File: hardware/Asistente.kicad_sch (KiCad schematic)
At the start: 11 parts, among them U2 pam8403

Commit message: hw: update PCB layout, add Gerber files and INMP441 footprint
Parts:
- C1: footprint (none) -> Capacitor_THT:CP_Radial_D10.0mm_P5.00mm
- C2, C3: footprint (none) -> Capacitor_SMD:C_0805_2012Metric
- INMP441: renamed from M1; footprint (none) -> INMP441:INMP441
- R3, R4: footprint (none) -> Resistor_SMD:R_0603_1608Metric
- U1: footprint ESP32_30pin -> ESP32_Footprints:ESP32_30pin
- U2: footprint (none) -> pam8403:pam8403
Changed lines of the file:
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@@
-		(color 0 0 0 0)
-	)
-	(junction
-		(at 85.09 106.68)
-		(diameter 0)
 		(color 0 0 0 0)
 	)
@@
 	(wire
 		(pts
-			(xy 83.82 106.68) (xy 85.09 106.68)
-		)
-		(stroke
-			(width 0)
-			(type default)
-		)
-	)
-	(wire
-		(pts
 			(xy 101.6 88.9) (xy 101.6 86.36)
 		)
@@
 	(wire
 		(pts
-			(xy 85.09 106.68) (xy 100.33 106.68)
-		)
-		(stroke
-			(width 0)
-			(type default)
-		)
-	)
-	(wire
-		(pts
 			(xy 140.97 44.45) (xy 140.97 33.02)
 		)
@@
 	(wire
 		(pts
+			(xy 83.82 106.68) (xy 100.33 106.68)
+		)
+		(stroke
+			(width 0)
+			(type default)
+		)
+	)
+	(wire
+		(pts
 			(xy 138.43 73.66) (xy 143.51 73.66)
 		)
@@
 		(pts
 			(xy 110.49 86.36) (xy 106.68 86.36)
-		)
-		(stroke
-			(width 0)
-			(type default)
-		)
-	)
-	(wire
-		(pts
-			(xy 85.09 105.41) (xy 85.09 106.68)
 		)
 		(stroke
@@
 			)
 		)
-		(property "Footprint" ""
+		(property "Footprint" "Resistor_SMD:R_0603_1608Metric"
 			(at 103.378 82.55 90)
 			(effects
@@
 			)
 		)
-		(property "Footprint" ""
+		(property "Footprint" "Capacitor_SMD:C_0805_2012Metric"
 			(at 96.52 72.39 0)
 			(effects
@@
 			)
 		)
-		(property "Footprint" ""
+		(property "Footprint" "Resistor_SMD:R_0603_1608Metric"
 			(at 98.298 82.55 90)
 			(effects
@@
 			)
 		)
-		(property "Footprint" ""
+		(property "Footprint" "Capacitor_THT:CP_Radial_D10.0mm_P5.00mm"
 			(at 101.2952 114.3 0)
 			(effects
@@
 			)
 		)
-		(property "Footprint" ""
+		(property "Footprint" "pam8403:pam8403"
 			(at 123.825 50.165 0)
 			(effects
@@
 			)
 		)
-		(property "Footprint" ""
+		(property "Footprint" "Capacitor_SMD:C_0805_2012Metric"
 			(at 101.6 72.39 0)
 			(effects
@@
 			)
 		)
-		(property "Footprint" "ESP32_30pin"
+		(property "Footprint" "ESP32_Footprints:ESP32_30pin"
 			(at 110.998 116.586 90)
 			(effects
@@
 				(path "/97dc264d-c8ec-4099-a14f-39f91d52d718"
 					(reference "U1")
-					(unit 1)
-				)
-			)
-		)
-	)
-	(symbol
-		(lib_id "power:PWR_FLAG")
-		(at 85.09 105.41 0)
-		(unit 1)
-		(exclude_from_sim no)
-		(in_bom yes)
-		(on_board yes)
-		(dnp no)
-		(fields_autoplaced yes)
-		(property "Reference" "#FLG01"
-			(at 85.09 103.505 0)
-			(effects
-				(font
-					(size 1.27 1.27)
-				)
-				(hide yes)
-			)
-		)
-		(property "Value" "PWR_FLAG"
-			(at 85.09 100.33 0)
-			(effects
-				(font
-					(size 1.27 1.27)
-				)
-			)
-		)
-		(property "Footprint" ""
-			(at 85.09 105.41 0)
-			(effects
-				(font
-					(size 1.27 1.27)
-				)
-				(hide yes)
-			)
-		)
-		(property "Datasheet" "~"
-			(at 85.09 105.41 0)
-			(effects
-				(font
-					(size 1.27 1.27)
-				)
-				(hide yes)
-			)
-		)
-		(property "Description" "Special symbol for telling ERC where power comes from"
-			(at 85.09 105.41 0)
-			(effects
-				(font
-					(size 1.27 1.27)
-				)
-				(hide yes)
-			)
-		)
-		(pin "1"
-		)
-		(instances
-			(project ""
-				(path "/97dc264d-c8ec-4099-a14f-39f91d52d718"
-					(reference "#FLG01")
 					(unit 1)
 				)
@@
 		(dnp no)
 		(fields_autoplaced yes)
-		(property "Reference" "M1"
+		(property "Reference" "INMP441"
 			(at 132.08 132.0799 0)
 			(effects
@@
 			)
 		)
-		(property "Footprint" ""
+		(property "Footprint" "INMP441:INMP441"
 			(at 124.46 133.35 0)
 			(effects
@@
 					(size 1.27 1.27)
 				)
-				(hide yes)
 			)
 		)
@@
 			(project ""
 				(path "/97dc264d-c8ec-4099-a14f-39f91d52d718"
-					(reference "M1")
+					(reference "INMP441")
 					(unit 1)
 				)

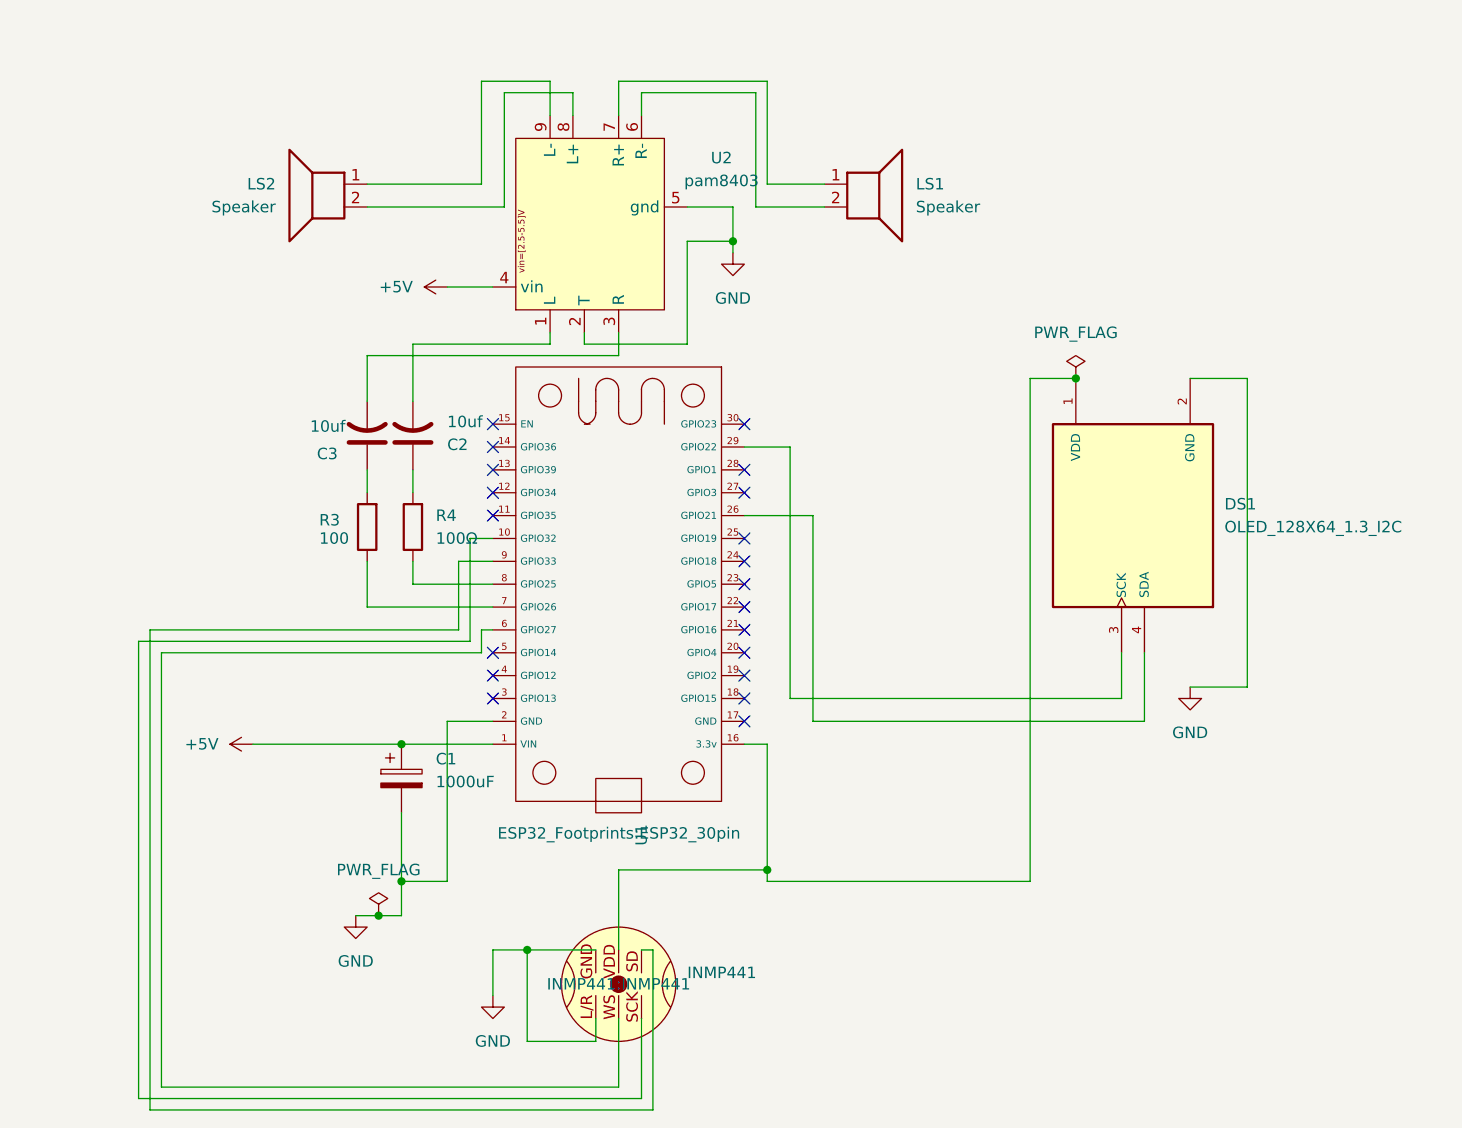
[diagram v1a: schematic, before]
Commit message: feat: add external connectors for OLED, mic and speakers, update gerber files
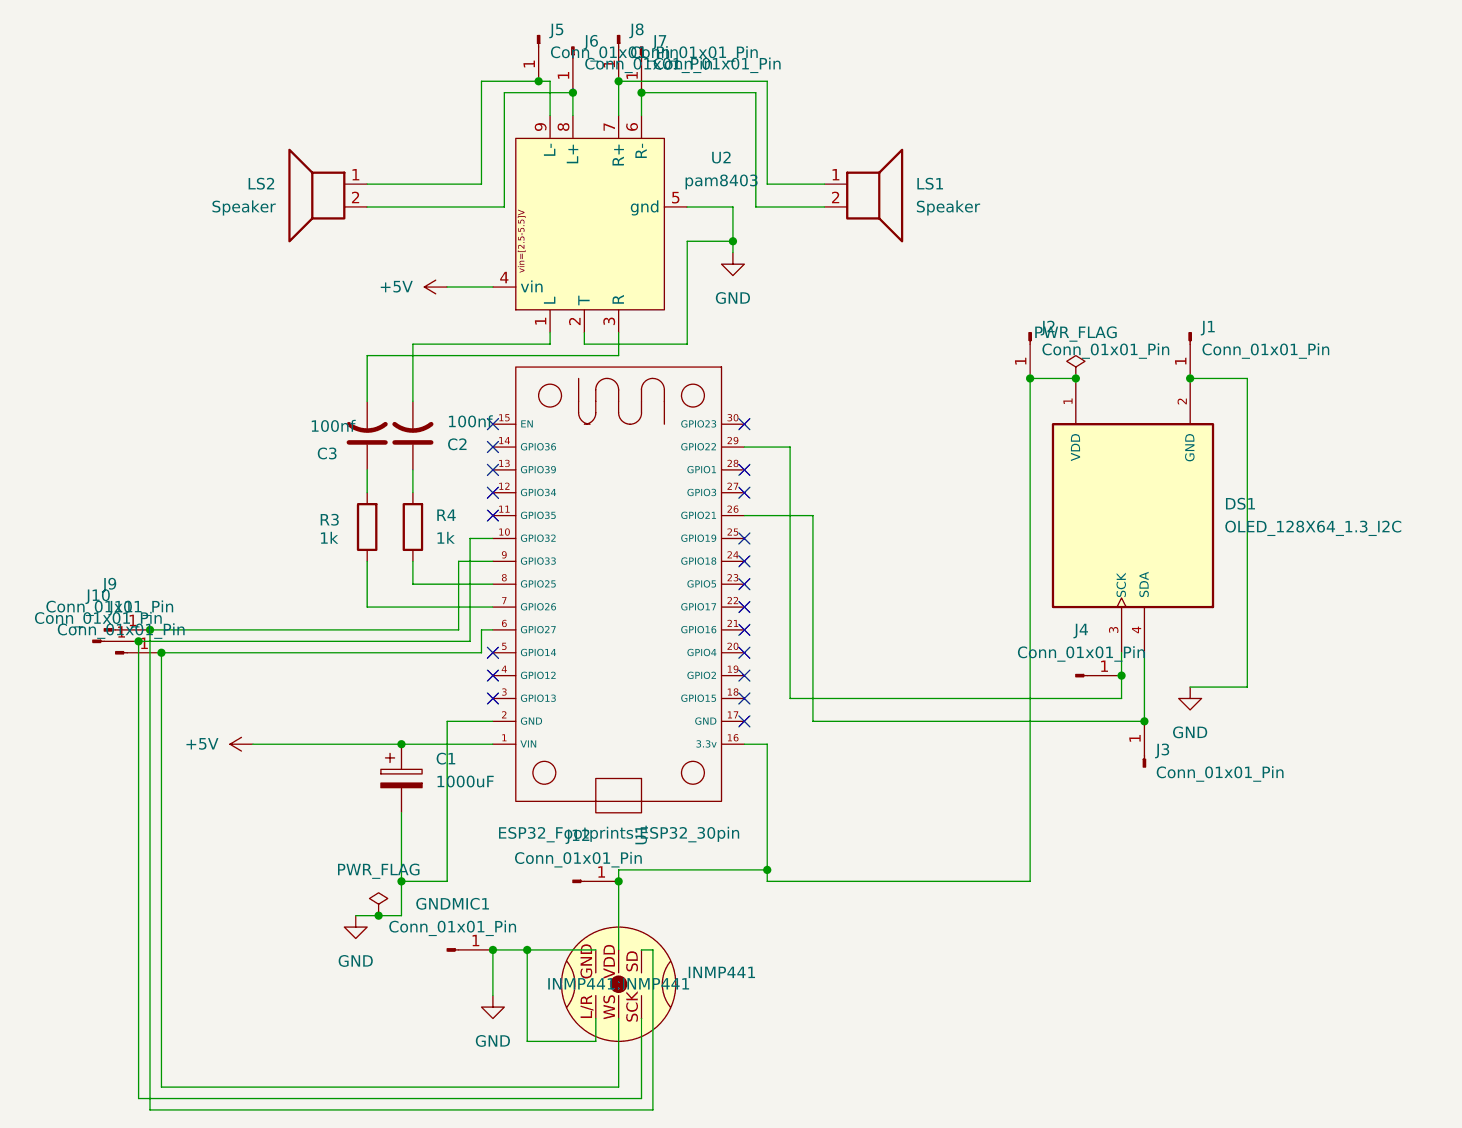
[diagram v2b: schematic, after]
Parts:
- added GNDMIC1, J1, J10, J11, J12, J2, J3, J4, J5, J6, J7, J8, J9: Conn_01x01_Pin, Connector_PinHeader_2.54mm:PinHeader_1x01_P2.54mm_Vertical, symbol Connector:Conn_01x01_Pin
- C2, C3: value 10uf -> 100nf
- R3: value 100 -> 1k
- R4: value 100Ω -> 1k
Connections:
- net GND: now also GNDMIC1.1 (Pin_1), J1.1 (Pin_1)
- net at LS2.1, U2.9 (L-): now also J5.1 (Pin_1)
- net at LS2.2, U2.8 (L+): now also J6.1 (Pin_1)
- net at LS1.2, U2.6 (R-): now also J7.1 (Pin_1)
- net at LS1.1, U2.7 (R+): now also J8.1 (Pin_1)
- net at DS1.1 (VDD), INMP441.VDD, U1.16 (3.3v): now also J12.1 (Pin_1), J2.1 (Pin_1)
- net at DS1.3 (SCK), U1.29 (GPIO22): now also J4.1 (Pin_1)
- net at DS1.4 (SDA), U1.26 (GPIO21): now also J3.1 (Pin_1)
- net at INMP441.SCK, U1.10 (GPIO32): now also J10.1 (Pin_1)
- net at INMP441.WS, U1.6 (GPIO27): now also J11.1 (Pin_1)
- net at INMP441.SD, U1.9 (GPIO33): now also J9.1 (Pin_1)
